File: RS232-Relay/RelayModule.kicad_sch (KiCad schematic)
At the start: 37 parts, among them K1 G5V-1, K2 G5V-1, K3 G5V-1, K4 G5V-1, Q1 2N3904, Q2 2N3904, Q3 2N3904, Q4 2N3904, U6 LTV-847S

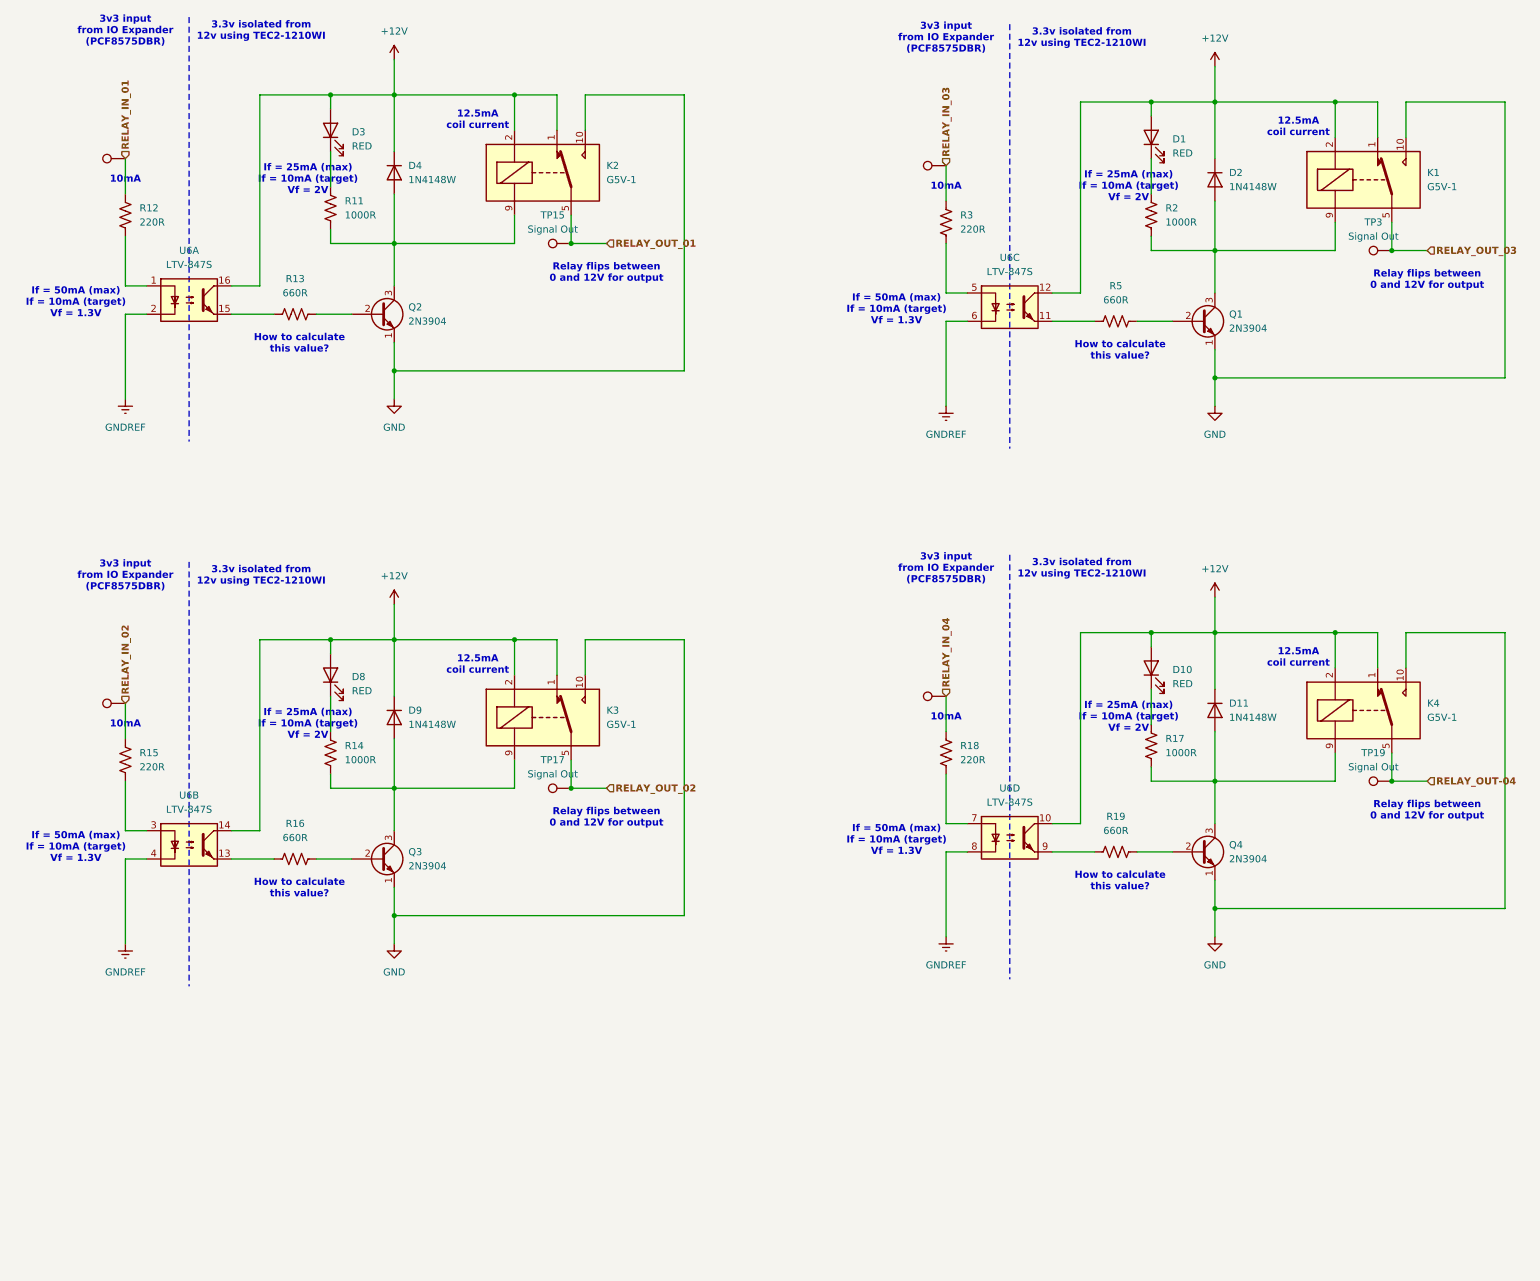
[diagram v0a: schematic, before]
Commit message: Pre-template layouts
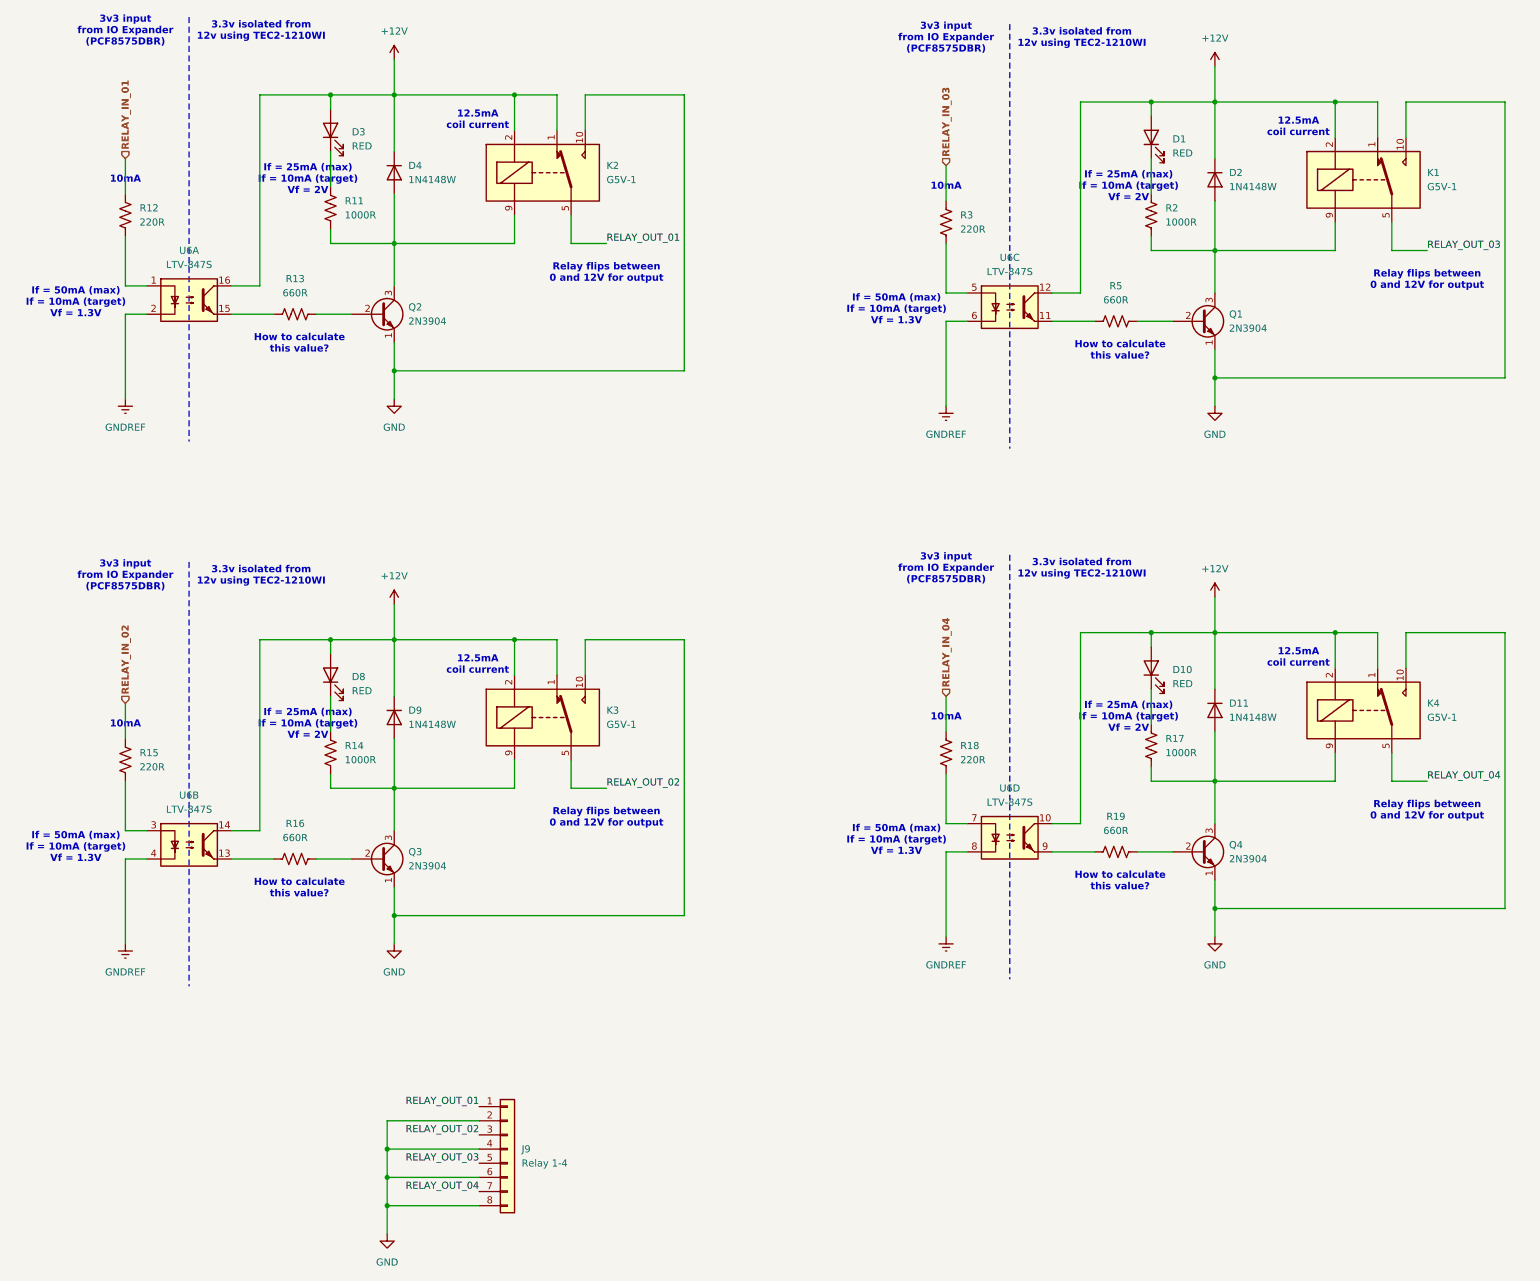
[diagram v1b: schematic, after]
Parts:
- removed TP14, TP16, TP18, TP2: Signal In, TestPoint:TestPoint_Pad_D1.0mm, symbol Connector:TestPoint
- removed TP15, TP17, TP19, TP3: Signal Out, TestPoint:TestPoint_Pad_D1.0mm, symbol Connector:TestPoint
- added J9: Relay 1-4, Connector_Phoenix_MSTB:PhoenixContact_MSTBA_2,5_8-G-5,08_1x08_P5.08mm_Horizontal, symbol Connector_Generic:Conn_01x08
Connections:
- net GND: now also J9.2 (Pin_2), J9.4 (Pin_4), J9.6 (Pin_6), J9.8 (Pin_8)
- net RELAY_OUT_01: now also J9.1 (Pin_1)
- net RELAY_OUT_02: now also J9.3 (Pin_3)
- net RELAY_OUT_03: now also J9.5 (Pin_5)
- net RELAY_OUT-04 renamed RELAY_OUT_04
- net RELAY_OUT_04: now also J9.7 (Pin_7)

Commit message: 1x Layout Complete
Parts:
- removed D1, D10, D3, D8: RED, LED_SMD:LED_0805_2012Metric, symbol Device:LED
- removed D11, D2, D4, D9: 1N4148W, Diode_SMD:D_SOD-123, symbol Device:D
- removed K1, K2, K3, K4: G5V-1, Relay_THT:Relay_SPDT_Omron_G5V-1, symbol Relay:G5V-1
- removed Q1, Q2, Q3, Q4: 2N3904, Package_TO_SOT_SMD:SOT-23, symbol Transistor_BJT:2N3904
- removed R11, R14, R17, R2: 1000R, Resistor_SMD:R_0603_1608Metric, symbol Device:R_US
- removed R12, R15, R18, R3: 220R, Resistor_SMD:R_0603_1608Metric, symbol Device:R_US
- removed R13, R16, R19, R5: 660R, Resistor_SMD:R_0603_1608Metric, symbol Device:R_US
- removed U6: LTV-847S, Package_DIP:SMDIP-16_W9.53mm, symbol Isolator:LTV-847S
- added U2: LTV-847S, Package_DIP:SMDIP-16_W9.53mm, symbol Isolator:LTV-847S
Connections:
- new net Relay-NO-ISO/OPTO_LEFT_IN: U2.7
- new net Relay-NO-ISO/OPTO_LEFT_OUT: U2.8
- new net Relay-NO-ISO/OPTO_RIGHT_IN: U2.10
- new net Relay-NO-ISO/OPTO_RIGHT_OUT: U2.9
- new net Relay-NO-ISO1/OPTO_LEFT_IN: U2.3
- new net Relay-NO-ISO1/OPTO_LEFT_OUT: U2.4
- new net Relay-NO-ISO1/OPTO_RIGHT_IN: U2.14
- new net Relay-NO-ISO1/OPTO_RIGHT_OUT: U2.13
- new net Relay-NO-ISO2/OPTO_LEFT_IN: U2.5
- new net Relay-NO-ISO2/OPTO_LEFT_OUT: U2.6
- new net Relay-NO-ISO2/OPTO_RIGHT_IN: U2.12
- new net Relay-NO-ISO2/OPTO_RIGHT_OUT: U2.11
- new net Relay-NO-ISO3/OPTO_LEFT_IN: U2.1
- new net Relay-NO-ISO3/OPTO_LEFT_OUT: U2.2
- new net Relay-NO-ISO3/OPTO_RIGHT_IN: U2.16
- new net Relay-NO-ISO3/OPTO_RIGHT_OUT: U2.15
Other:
- added sheet Relay-NO-ISO (Relay-NO-ISO.kicad_sch)
- added sheet Relay-NO-ISO1 (Relay-NO-ISO.kicad_sch)
- added sheet Relay-NO-ISO2 (Relay-NO-ISO.kicad_sch)
- added sheet Relay-NO-ISO3 (Relay-NO-ISO.kicad_sch)
- note removed: "10mA"
- note removed: "12.5mA coil current"
- note removed: "3.3v isolated from 12v using TEC2-1210WI"
- note removed: "3v3 input from IO Expander (PCF8575DBR)"
- note removed: "How to calculate this value?"
- note removed: "If = 25mA (max) If = 10mA (target) Vf = 2V"
- note removed: "If = 50mA (max) If = 10mA (target) Vf = 1.3V"
- note removed: "Relay flips between 0 and 12V for output"

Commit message: Routing Complete (vias next)
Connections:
- net Relay-NO-ISO1/OPTO_LEFT_IN: now also U2.5; no longer U2.3
- net Relay-NO-ISO1/OPTO_LEFT_OUT: now also U2.6; no longer U2.4
- net Relay-NO-ISO1/OPTO_RIGHT_IN: now also U2.12; no longer U2.14
- net Relay-NO-ISO1/OPTO_RIGHT_OUT: now also U2.11; no longer U2.13
- net Relay-NO-ISO2/OPTO_LEFT_IN: now also U2.3; no longer U2.5
- net Relay-NO-ISO2/OPTO_LEFT_OUT: now also U2.4; no longer U2.6
- net Relay-NO-ISO2/OPTO_RIGHT_IN: now also U2.14; no longer U2.12
- net Relay-NO-ISO2/OPTO_RIGHT_OUT: now also U2.13; no longer U2.11
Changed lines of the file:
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@@
 	(symbol
 		(lib_id "Isolator:LTV-847S")
-		(at 130.81 142.24 0)
+		(at 130.81 102.87 0)
 		(unit 3)
 		(exclude_from_sim no)
@@
 		(fields_autoplaced yes)
 		(property "Reference" "U2"
-			(at 130.81 133.35 0)
+			(at 130.81 93.98 0)
 			(effects
 				(font
@@
 		)
 		(property "Value" "LTV-847S"
-			(at 130.81 135.89 0)
+			(at 130.81 96.52 0)
 			(effects
 				(font
@@
 		)
 		(property "Footprint" "Package_DIP:SMDIP-16_W9.53mm"
-			(at 130.81 149.86 0)
+			(at 130.81 110.49 0)
 			(effects
 				(font
@@
 		)
 		(property "Datasheet" "http://www.us.liteon.com/downloads/LTV-817-827-847.PDF"
-			(at 115.57 130.81 0)
+			(at 115.57 91.44 0)
 			(effects
 				(font
@@
 		)
 		(property "Description" "DC Optocoupler, Vce 35V, CTR 50%, SMDIP-16"
-			(at 130.81 142.24 0)
+			(at 130.81 102.87 0)
 			(effects
 				(font
@@
 	)
 	(symbol
-		(lib_id "Isolator:LTV-847S")
-		(at 130.81 102.87 0)
-		(unit 2)
-		(exclude_from_sim no)
-		(in_bom yes)
-		(on_board yes)
-		(dnp no)
-		(fields_autoplaced yes)
-		(property "Reference" "U2"
-			(at 130.81 93.98 0)
-			(effects
-				(font
-					(size 1.27 1.27)
-				)
-			)
-		)
-		(property "Value" "LTV-847S"
-			(at 130.81 96.52 0)
-			(effects
-				(font
-					(size 1.27 1.27)
-				)
-			)
-		)
-		(property "Footprint" "Package_DIP:SMDIP-16_W9.53mm"
-			(at 130.81 110.49 0)
-			(effects
-				(font
-					(size 1.27 1.27)
-				)
-				(hide yes)
-			)
-		)
-		(property "Datasheet" "http://www.us.liteon.com/downloads/LTV-817-827-847.PDF"
-			(at 115.57 91.44 0)
-			(effects
-				(font
-					(size 1.27 1.27)
-				)
-				(hide yes)
-			)
-		)
-		(property "Description" "DC Optocoupler, Vce 35V, CTR 50%, SMDIP-16"
-			(at 130.81 102.87 0)
-			(effects
-				(font
-					(size 1.27 1.27)
-				)
-				(hide yes)
-			)
-		)
-		(pin "10"
-		)
-		(pin "4"
-		)
-		(pin "7"
-		)
-		(pin "6"
-		)
-		(pin "8"
-		)
-		(pin "16"
-		)
-		(pin "12"
-		)
-		(pin "1"
-		)
-		(pin "15"
-		)
-		(pin "14"
-		)
-		(pin "3"
-		)
-		(pin "11"
-		)
-		(pin "2"
-		)
-		(pin "9"
-		)
-		(pin "13"
-		)
-		(pin "5"
-		)
-		(instances
-			(project "RS232-Relay"
-				(path "/6e416d74-c18a-4d9a-a47c-4314aa8f470f/6243990a-47f3-4383-9005-5094cba86ad2"
-					(reference "U2")
-					(unit 2)
-				)
-				(path "/6e416d74-c18a-4d9a-a47c-4314aa8f470f/4cc60208-aa63-44fd-9447-92e9d40fbb60"
-					(reference "U5")
-					(unit 2)
-				)
-				(path "/6e416d74-c18a-4d9a-a47c-4314aa8f470f/f5401bb4-9575-46b7-b322-a153ebcf6229"
-					(reference "U6")
-					(unit 2)
-				)
-			)
-		)
-	)
-	(symbol
 		(lib_id "power:GND")
 		(at 144.78 248.92 0)
@@
 				)
 			)
+		)
+	)
+	(symbol
+		(lib_id "Isolator:LTV-847S")
+		(at 130.81 142.24 0)
+		(unit 2)
+		(exclude_from_sim no)
+		(in_bom yes)
+		(on_board yes)
+		(dnp no)
+		(fields_autoplaced yes)
+		(property "Reference" "U2"
+			(at 130.81 133.35 0)
+			(effects
+				(font
+					(size 1.27 1.27)
+				)
+			)
+		)
+		(property "Value" "LTV-847S"
+			(at 130.81 135.89 0)
+			(effects
+				(font
+					(size 1.27 1.27)
+				)
+			)
+		)
+		(property "Footprint" "Package_DIP:SMDIP-16_W9.53mm"
+			(at 130.81 149.86 0)
+			(effects
+				(font
+					(size 1.27 1.27)
+				)
+				(hide yes)
+			)
+		)
+		(property "Datasheet" "http://www.us.liteon.com/downloads/LTV-817-827-847.PDF"
+			(at 115.57 130.81 0)
+			(effects
+				(font
+					(size 1.27 1.27)
+				)
+				(hide yes)
+			)
+		)
+		(property "Description" "DC Optocoupler, Vce 35V, CTR 50%, SMDIP-16"
+			(at 130.81 142.24 0)
+			(effects
+				(font
+					(size 1.27 1.27)
+				)
+				(hide yes)
+			)
+		)
+		(pin "10"
+		)
+		(pin "4"
+		)
+		(pin "7"
+		)
+		(pin "6"
+		)
+		(pin "8"
+		)
+		(pin "16"
+		)
+		(pin "12"
+		)
+		(pin "1"
+		)
+		(pin "15"
+		)
+		(pin "14"
+		)
+		(pin "3"
+		)
+		(pin "11"
+		)
+		(pin "2"
+		)
+		(pin "9"
+		)
+		(pin "13"
+		)
+		(pin "5"
+		)
+		(instances
+			(project "RS232-Relay"
+				(path "/6e416d74-c18a-4d9a-a47c-4314aa8f470f/6243990a-47f3-4383-9005-5094cba86ad2"
+					(reference "U2")
+					(unit 2)
+				)
+				(path "/6e416d74-c18a-4d9a-a47c-4314aa8f470f/4cc60208-aa63-44fd-9447-92e9d40fbb60"
+					(reference "U5")
+					(unit 2)
+				)
+				(path "/6e416d74-c18a-4d9a-a47c-4314aa8f470f/f5401bb4-9575-46b7-b322-a153ebcf6229"
+					(reference "U6")
+					(unit 2)
+				)
+			)

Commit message: Production v1
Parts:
- J9: LCSC (none) -> C114599
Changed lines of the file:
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@@
+			)
+		)
+		(property "LCSC" "C114599"
+			(at 166.37 233.68 0)
+			(effects
+				(font
+					(size 1.27 1.27)
+				)
+				(hide yes)
 			)
 		)
